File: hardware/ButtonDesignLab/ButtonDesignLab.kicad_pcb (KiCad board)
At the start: 2 copper layers, 25 x 25 mm, 6 parts, among them J1 Conn_01x02, SW1 SW_Push

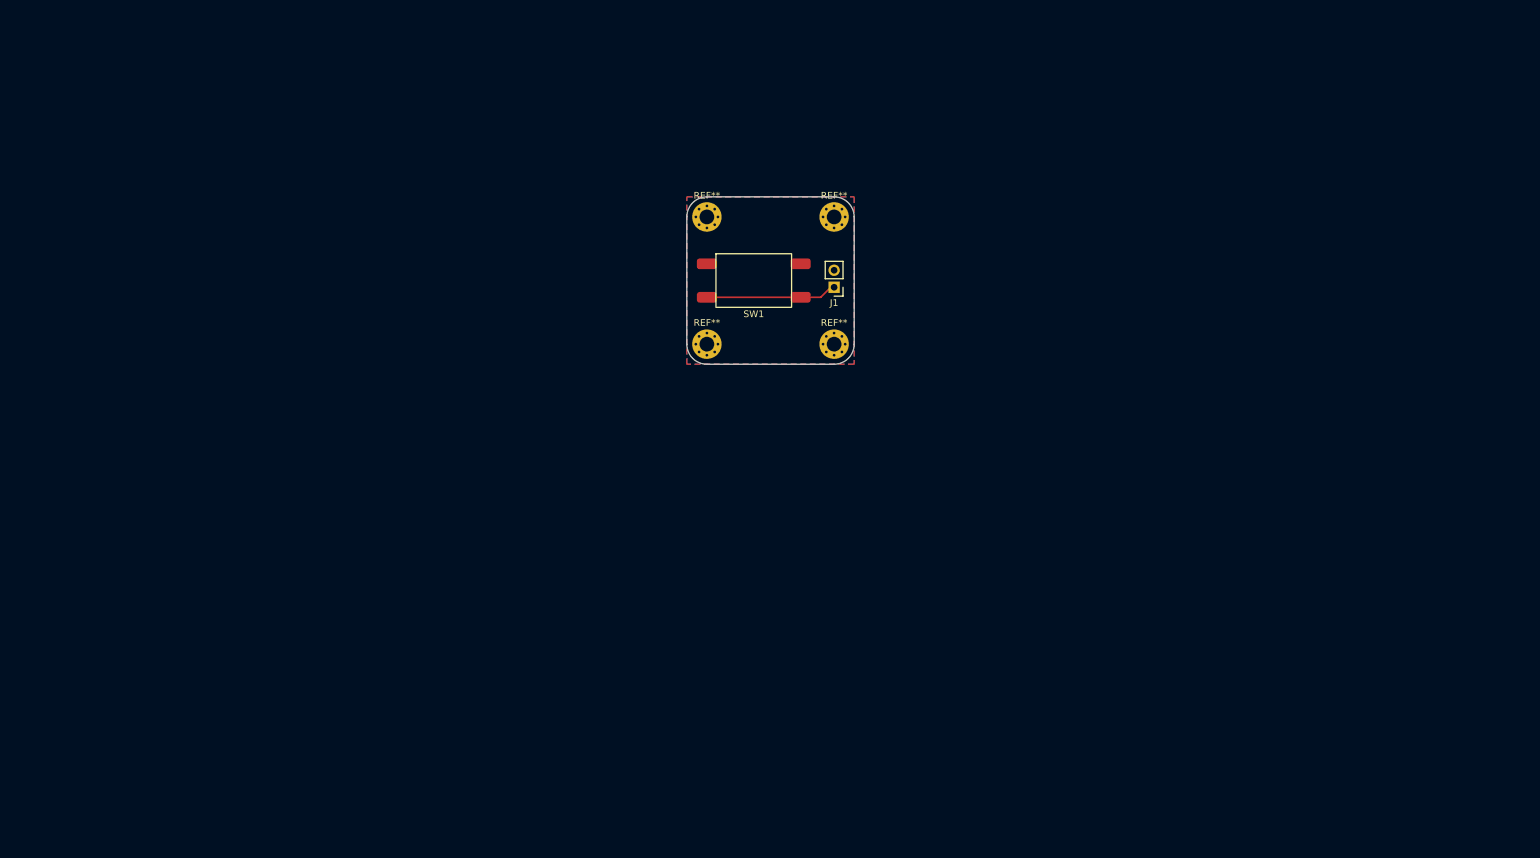
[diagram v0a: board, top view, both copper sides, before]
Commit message: Almost finished the PCB  and started with the PCB of buttons
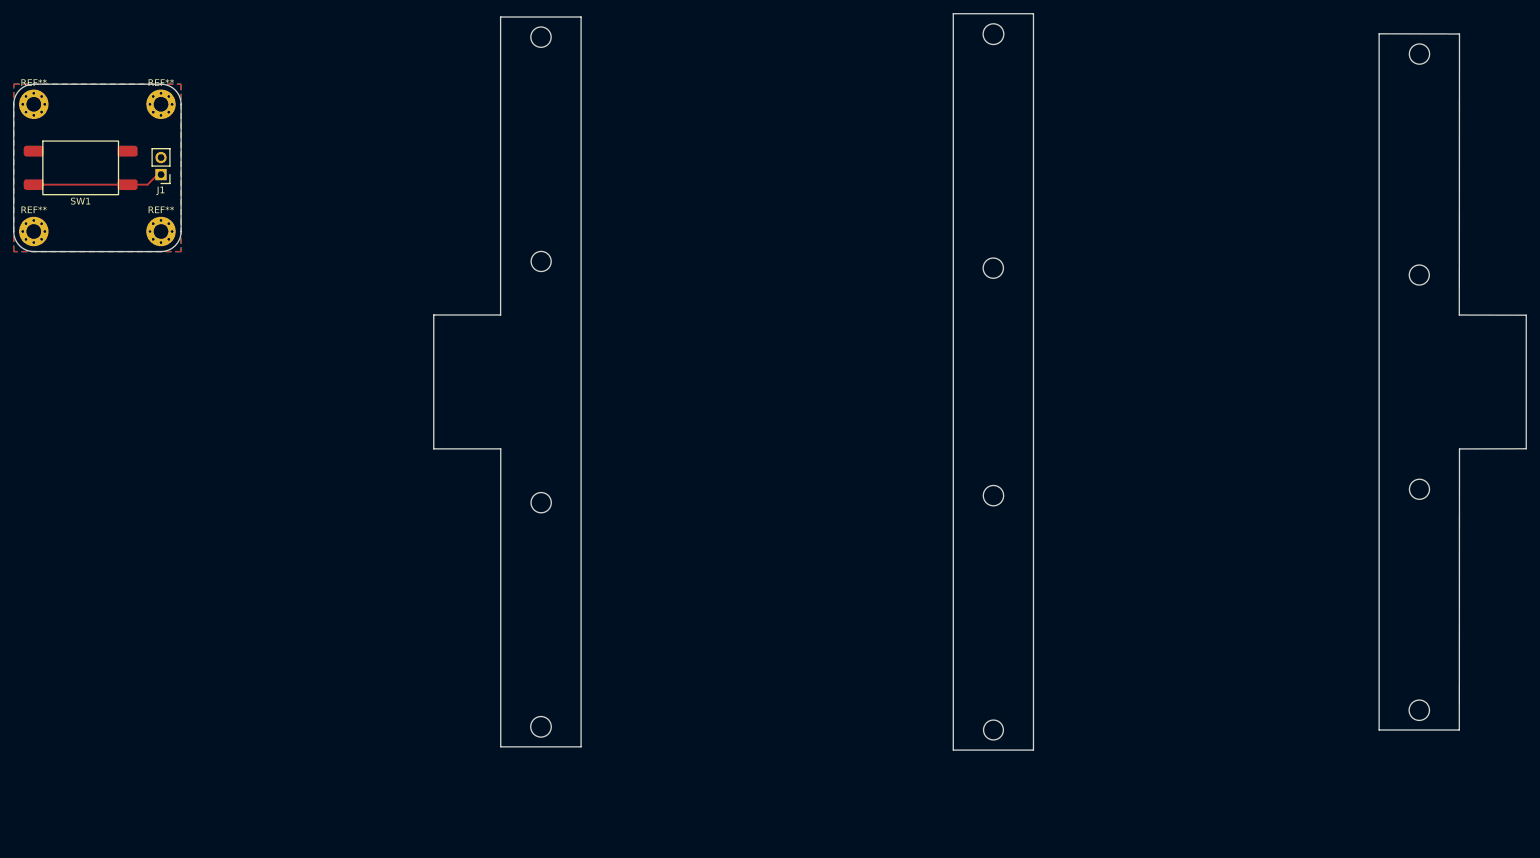
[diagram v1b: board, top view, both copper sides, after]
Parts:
- moved J1 101.9 mm to (46.5, 44.7)
- moved REF** 101.9 mm to (46.5, 34.2)
- moved REF** 101.9 mm to (27.5, 34.2)
- moved REF** 101.9 mm to (27.5, 53.2)
- moved REF** 101.9 mm to (46.5, 53.2)
- moved SW1 101.9 mm to (34.5, 43.7)
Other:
- board size 25 x 25 mm -> 225.9 x 110 mm
- board text added: "Front Left PCB"
- board text added: "Front Right PCB"

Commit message: Finished button PCBs
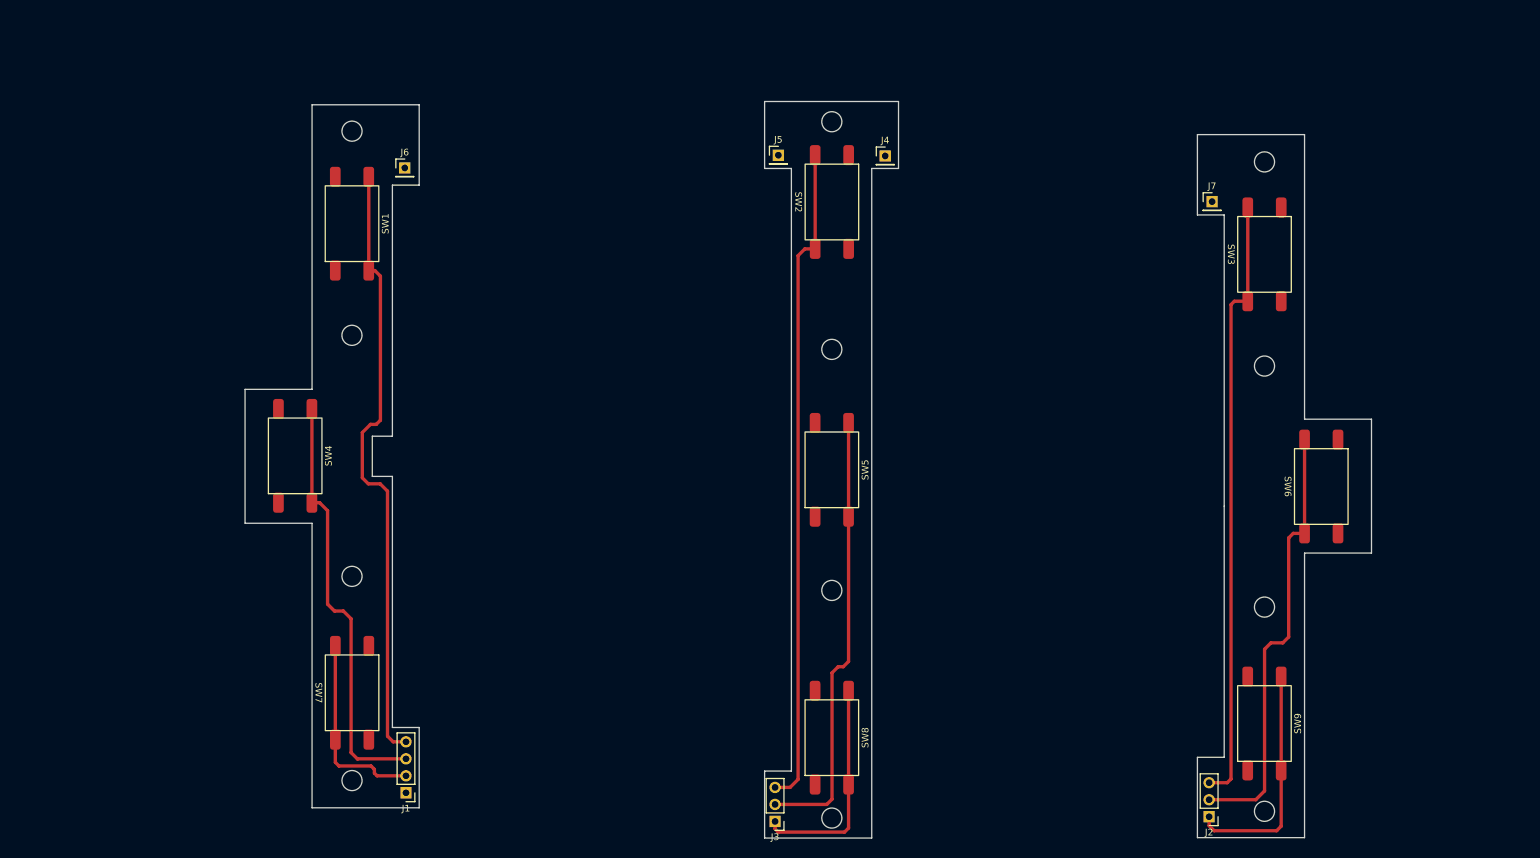
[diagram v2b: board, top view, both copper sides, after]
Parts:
- removed REF** (x4): MountingHole_2.2mm_M2_Pad_Via, MountingHole:MountingHole_2.2mm_M2_Pad_Via
- added J2: Conn_01x03, Connector_PinHeader_2.54mm:PinHeader_1x03_P2.54mm_Vertical, F.Cu at (203.0, 140.6)
- added J3: Conn_01x03, Connector_PinHeader_2.54mm:PinHeader_1x03_P2.54mm_Vertical, F.Cu at (138.2, 141.3)
- added J4: Conn_01x01, Connector_PinHeader_2.54mm:PinHeader_1x01_P2.54mm_Vertical, F.Cu at (154.6, 41.9)
- added J5: Conn_01x01, Connector_PinHeader_2.54mm:PinHeader_1x01_P2.54mm_Vertical, F.Cu at (138.7, 41.8)
- added J6: Conn_01x01, Connector_PinHeader_2.54mm:PinHeader_1x01_P2.54mm_Vertical, F.Cu at (82.9, 43.7)
- added J7: Conn_01x01, Connector_PinHeader_2.54mm:PinHeader_1x01_P2.54mm_Vertical, F.Cu at (203.4, 48.7)
- added SW2: SW_Push, Design:Button, F.Cu at (146.7, 48.8)
- added SW3: SW_Push, Design:Button, F.Cu at (211.3, 56.6)
- added SW4: SW_Push, Design:Button, F.Cu at (66.5, 86.7)
- added SW5: SW_Push, Design:Button, F.Cu at (146.7, 88.8)
- added SW6: SW_Push, Design:Button, F.Cu at (219.8, 91.3)
- added SW7: SW_Push, Design:Button, F.Cu at (75.0, 122.1)
- added SW8: SW_Push, Design:Button, F.Cu at (146.7, 128.8)
- added SW9: SW_Push, Design:Button, F.Cu at (211.3, 126.7)
- J1: value Conn_01x02 -> Conn_01x04; footprint Connector_PinHeader_2.54mm:PinHeader_1x02_P2.54mm_Vertical -> Connector_PinHeader_2.54mm:PinHeader_1x04_P2.54mm_Vertical
- moved J1 99.3 mm to (83.1, 137.0)
- moved SW1 41.4 mm to (75.0, 52.0), turned to 90 degrees
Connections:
- J1 pad 1: /SIGNAL -> /GND
- J1 pad 2: /GND -> /D6
- SW1 pad 2: /SIGNAL -> /D0
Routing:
- net /D1: track 0.00 -> 99.1 mm
- net /D0: track 0.00 -> 92.1 mm
- net /D2: track 0.00 -> 91.1 mm
- net /D4: track 0.00 -> 66.5 mm
- net /D5: track 0.00 -> 65.8 mm
- net /D3: track 0.00 -> 63.8 mm
- net /D8: track 0.00 -> 35.0 mm
- net /D7: track 0.00 -> 33.0 mm
- net /D6: track 0.00 -> 29.1 mm
- net /SIGNAL: track 19.6 -> 0.00 mm
- removed copper zone on B.Cu, net /GND
- removed copper zone on F.Cu, net /GND
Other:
- board size 225.9 x 110 mm -> 168.2 x 110 mm
- board text removed: "Front Left PCB"
- board text removed: "Front Right PCB"
